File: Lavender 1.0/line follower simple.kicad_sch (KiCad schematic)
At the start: 51 parts, among them J1 XT60-M, J2 Conn_01x09_Pin, J3 Conn_01x02_Socket, J4 Conn_01x02_Socket, J5 Conn_01x09_Pin, J7 Conn_01x09_Socket, U10 QRE1113GR, U11 QRE1113GR, U12 STM32F411CEUx, U2 TCRT5000L, U3 QRE1113GR, U4 QRE1113GR, U5 QRE1113GR, U6 QRE1113GR, U7 QRE1113GR, U8 QRE1113GR, U9 QRE1113GR

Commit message: Added switches
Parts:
- removed BT1: ~, symbol customs:HC-05
- removed C10, C11, C18, C19, C20, C21, C22, C23, C9: 0.1u, symbol Device:C_Small
- removed J2: Conn_01x09_Pin, symbol Connector:Conn_01x09_Pin
- removed MP1: ~, symbol customs:MP1584
- removed R10, R12, R16, R18, R2, R4, R9: 220, symbol Device:R_Small
- removed R11, R13, R14, R15, R17, R3: 100, symbol Device:R_Small
- removed TB1: ~, symbol customs:tb6612_module
- removed U1: ~, symbol customs:Blackpill
- removed U12: STM32F411CEUx, Package_DFN_QFN:QFN-48-1EP_7x7mm_P0.5mm_EP5.6x5.6mm, symbol MCU_ST_STM32F4:STM32F411CEUx
- removed U3, U4, U5, U6, U7, U8, U9: QRE1113GR, QRE1113GR:SOIC180P460X187-4N, symbol customs:QRE1113GR
- added BT2: (no value), symbol customs:HC-05
- added JP1: SolderJumper_2_Open, symbol Jumper:SolderJumper_2_Open
- added MP2: (no value), symbol customs:MP1584
- added R24, R25, R27, R29, R32, R35, R38, R41, R44: 10k, symbol Device:R_Small
- added R26, R28, R31, R34, R37, R40, R43: 150, symbol Device:R_Small
- added R30, R33, R36, R39, R42, R45: 220, symbol Device:R_Small
- added SW1: SW_DPDT_x2, symbol Switch:SW_DPDT_x2
- added SW2: SW_Push, symbol Switch:SW_Push
- added TB2: (no value), symbol customs:tb6612_module
- added U1: YAAJ_BlackPill_Part_Like_SWD_Breakout, symbol customs:YAAJ_BlackPill_Part_Like_SWD_Breakout
- added U12, U13, U14, U15, U16, U17, U18: QRE1113GR, QRE1113GR:SOIC180P460X187-4N, symbol customs:QRE1113GR
- R21: value 100 -> 220
- R22, R23: value 100 -> 150
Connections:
- net +3.3V: now also BT2. (EN), MP2. (IN+), R24.2, R25.2, R26.2, R27.2, R28.2, R29.2, R31.2, R32.2, R34.2, R35.2, R37.2, R38.2, R40.2, R41.2, R43.2, R44.2, TB2. (M1Out+); no longer R21.2
- net BAT+: now also SW1.2 (B)
- net GND: now also BT2. (EN), MP2. (IN+), SW2.1, TB2. (M1Out+), U12.2, U12.4, U13.2, U13.4, U14.2, U14.4, U15.2, U15.4, U16.2, U16.4, U17.2, U17.4, U18.2, U18.4
- net Motor1+: now also TB2. (M1Out+)
- net Motor1-: now also TB2. (M1Out+)
- net Motor2+: now also TB2. (M1Out+)
- net Motor2-: now also TB2. (M1Out+)
- net PIN: now also BT2. (EN)
- net Q1: now also R19.1, JP1.1 (A); no longer J5.9 (Pin_9)
- net Q2: now also R20.1; no longer J5.8 (Pin_8)
- net Q3: now also R21.1; no longer J5.7 (Pin_7)
- net Q4: now also R30.1; no longer J5.6 (Pin_6)
- net Q5: now also R33.1; no longer J5.5 (Pin_5)
- net Q6: now also R36.1; no longer J5.4 (Pin_4)
- net Q7: now also R39.1; no longer J5.3 (Pin_3)
- net Q8: now also R42.1; no longer J5.2 (Pin_2), R19.1
- net Q9: now also R45.1; no longer J5.1 (Pin_1), R20.1
- net at R19.2, U10.3: now also R24.1
- net at R20.2, U11.3: now also R25.1
- net BAT_SNS renamed PB1
- net PB1: now also U1.32 (PB1)
- removed net Pin: J7.1 (Pin_1), J7.2 (Pin_2), J7.3 (Pin_3), J7.4 (Pin_4), J7.5 (Pin_5), J7.6 (Pin_6), J7.7 (Pin_7), J7.8 (Pin_8), J7.9 (Pin_9)
- new net: R32.1, R33.2, U14.3
- new net: R38.1, R39.2, U16.3
- new net: R40.1, U17.1
- new net: R29.1, R30.2, U13.3
- new net: R41.1, R42.2, U17.3
- new net: R26.1, U12.1
- new net: R43.1, U18.1
- new net: R44.1, R45.2, U18.3
- new net: R28.1, U13.1
- new net: R31.1, U14.1
- new net: R37.1, U16.1
- new net: J5.9 (Pin_9), JP1.2 (B)
- new net: R21.2, R27.1, U12.3
- new net: R34.1, U15.1
- new net: R35.1, R36.2, U15.3
- new net BAT+_Driver: SW1.4 (A), TB2. (M1Out+)
- new net BAT+_out: MP2. (IN+), SW1.1 (A), SW1.5 (B)
- new net PA0: J7.9 (Pin_9), U1.23 (PA0)
- new net PA1: J7.8 (Pin_8), U1.24 (PA1)
- new net PA10: BT2. (EN), U1.7 (PA10)
- new net PA11: TB2. (M1Out+), U1.8 (PA11)
- new net PA2: J7.7 (Pin_7), U1.25 (PA2)
- new net PA3: J7.6 (Pin_6), U1.26 (PA3)
- new net PA4: J7.5 (Pin_5), U1.27 (PA4)
- new net PA5: J7.4 (Pin_4), U1.28 (PA5)
- new net PA6: J7.3 (Pin_3), U1.29 (PA6)
- new net PA7: J7.2 (Pin_2), U1.30 (PA7)
- new net PA8: TB2. (M1Out+), U1.5 (PA8)
- new net PA9: BT2. (EN), U1.6 (PA9)
- new net PB0: J7.1 (Pin_1), U1.31 (PB0)
- new net PB12: TB2. (M1Out+), U1.1 (PB12)
- new net PB13: TB2. (M1Out+), U1.2 (PB13)
- new net PB14: TB2. (M1Out+), U1.3 (PB14)
- new net PB15: TB2. (M1Out+), U1.4 (PB15)
- new net PB4: SW2.2, U1.12 (PB4)
- no-connect marks 0 -> 6
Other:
- moved on the sheet: J5, J7, U2

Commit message: Completed schematic layout
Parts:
- removed J1: XT60-M, XT60-M:AMASS_XT60-M, symbol New_Library:XT60-M
- removed J5: Conn_01x09_Pin, symbol Connector:Conn_01x09_Pin
- removed J7: Conn_01x09_Socket, symbol Connector:Conn_01x09_Socket
- removed MP2: (no value), symbol customs:MP1584
- removed U1: YAAJ_BlackPill_Part_Like_SWD_Breakout, symbol customs:YAAJ_BlackPill_Part_Like_SWD_Breakout
- added BlackPill1: STM32F411_BP, ROBO:STM32F411-BP, symbol RM_Footprints:STM32F411-BlackPill
- added J1: XT30UPB-M, XT30UPB-M:AMASS_XT30UPB-M, symbol customs:XT30UPB-M
- added J6, J7: Conn_02x06_Counter_Clockwise, symbol Connector_Generic:Conn_02x06_Counter_Clockwise
- added JP10, JP11, JP12, JP13, JP14, JP15, JP16, JP17, JP18, JP19, JP2, JP20, JP3, JP4, JP5, JP6, JP7, JP8, JP9: SolderJumper_2_Open, symbol Jumper:SolderJumper_2_Open
- added MP1: (no value), symbol customs:MP1584
- added R49, R52, R55, R58, R61, R64, R67, R70, R73: 150, symbol Device:R_Small
- added R50, R53, R56, R59, R62, R65, R68, R71, R74: 4k7, symbol Device:R_Small
- added R51, R54, R57, R60, R63, R66, R69, R72, R75: 220, symbol Device:R_Small
- added U19, U20, U4, U5, U6, U7, U8, U9: TCRT5000L, TCRT5000L:XDCR_TCRT5000L, symbol customs:TCRT5000L
- added U3: 2472, 2472:MODULE_2472, symbol customs:2472
- R24, R25, R27, R29, R32, R35, R38, R41, R44: value 10k -> 4k7
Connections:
- net PA11 is gone; now on net PWMB: TB2. (M1Out+)
- net PA8 is gone; now on net PWMB: TB2. (M1Out+)
- net PA9 is gone; now on net TXD: BT2. (EN)
- net PB12 is gone; now on net PWMB: TB2. (M1Out+)
- net PB13 is gone; now on net PWMB: TB2. (M1Out+)
- net PB14 is gone; now on net PWMB: TB2. (M1Out+)
- net PB15 is gone; now on net PWMB: TB2. (M1Out+)
- net PIN is gone; now on net TXD: BT2. (EN)
- net +3.3V: now also BlackPill1.40 (3V3), J6.7 (Pin_7), J7.7 (Pin_7), JP19.2 (B), JP20.2 (B), MP1. (IN+), U3.1 (VIN); no longer R22.2, R23.2, R24.2, R25.2, R26.2, R27.2, R28.2, R29.2, R31.2, R32.2, R34.2, R35.2, R37.2, R38.2, R40.2, R41.2, R43.2, R44.2
- net BAT+: now also J1.P
- net BAT+_out: now also MP1. (IN+)
- net GND: now also U2.2, U2.3, BlackPill1.2 (GND), BlackPill1.39 (GND), J1.N, J6.6 (Pin_6), J7.6 (Pin_6), MP1. (IN+), U19.2, U19.3, U20.2, U20.3, U3.10 (PS0), U3.3 (GND), U3.7 (ADR), U3.9 (PS1), U4.2, U4.3, U5.2, U5.3, U6.2, U6.3, U7.2, U7.3, U8.2, U8.3, U9.2, U9.3
- net Q1: now also JP2.1 (A); no longer JP1.1 (A)
- net Q2: now also JP4.1 (A)
- net Q3: now also JP6.1 (A)
- net Q4: now also JP8.1 (A)
- net Q5: now also JP10.1 (A)
- net Q6: now also JP11.1 (A)
- net Q7: now also JP14.1 (A)
- net Q8: now also JP16.1 (A)
- net Q9: now also JP18.1 (A)
- net T1: now also JP1.1 (A), R51.2
- net T2: now also JP3.1 (A), R54.2
- net T3: now also JP5.1 (A), R57.2
- net T4: now also JP7.1 (A), R60.2
- net T5: now also JP9.1 (A), R63.2
- net T6: now also JP12.1 (A), R66.2
- net T7: now also JP13.1 (A), R69.2
- net T8: now also JP15.1 (A), R72.2
- net T9: now also JP17.1 (A), R75.2
- net at U2.1: now also R50.2, R51.1
- net at U2.4: now also R49.2
- net at JP1.2 (B): now also J6.1 (Pin_1), JP2.2 (B)
- net PWMB: now reaches TB2. (M1Out+)
- net PWMB: now also BlackPill1.28 (PA11)
- net PA10 renamed TXD
- net TXD: now also BlackPill1.27 (PA10)
- net PB1 renamed BAT_SNS
- net BAT_SNS: now also BlackPill1.6 (PB1)
- net PB4 renamed Button
- net Button: now also BlackPill1.32 (PB4)
- new net: J6.10 (Pin_10), JP15.2 (B), JP16.2 (B)
- new net: J6.11 (Pin_11), JP13.2 (B), JP14.2 (B)
- new net: R56.2, R57.1, U5.1
- new net: R55.2, U5.4
- new net: R68.2, R69.1, U9.1
- new net: J6.5 (Pin_5), JP10.2 (B), JP9.2 (B)
- new net: J6.3 (Pin_3), JP5.2 (B), JP6.2 (B)
- new net: R65.2, R66.1, U8.1
- new net: R64.2, U8.4
- new net: R67.2, U9.4
- new net: J6.12 (Pin_12), JP11.2 (B), JP12.2 (B)
- new net: R71.2, R72.1, U19.1
- new net: R70.2, U19.4
- new net: J6.2 (Pin_2), JP3.2 (B), JP4.2 (B)
- new net: J6.4 (Pin_4), JP7.2 (B), JP8.2 (B)
- new net: J6.9 (Pin_9), JP17.2 (B), JP18.2 (B)
- new net: R62.2, R63.1, U7.1
- new net: R61.2, U7.4
- new net: R74.2, R75.1, U20.1
- new net: R73.2, U20.4
- new net: R59.2, R60.1, U6.1
- new net: R58.2, U6.4
- new net: R53.2, R54.1, U4.1
- new net: R52.2, U4.4
- new net AIN1: BlackPill1.23 (PB14), TB2. (M1Out+)
- new net AIN2: BlackPill1.24 (PB15), TB2. (M1Out+)
- new net BIN1: BlackPill1.22 (PB13), TB2. (M1Out+)
- new net BIN2: BlackPill1.21 (PB12), TB2. (M1Out+)
- new net EN: BT2. (EN), BlackPill1.34 (PB6)
- new net IMU_RST: BlackPill1.4 (PB10), U3.6 (RST)
- new net IMU_SCL: BlackPill1.36 (PB8), U3.5 (SCL)
- new net IMU_SDA: BlackPill1.37 (PB9), U3.4 (SDA)
- new net PWMA: BlackPill1.25 (PA8), TB2. (M1Out+)
- new net Q_PWR: JP19.1 (A), R22.2, R23.2, R24.2, R25.2, R26.2, R27.2, R28.2, R29.2, R31.2, R32.2, R34.2, R35.2, R37.2, R38.2, R40.2, R41.2, R43.2, R44.2
- new net RXD: BT2. (EN), BlackPill1.26 (PA9)
- new net SNSR1: BlackPill1.15 (PA0), J7.1 (Pin_1)
- new net SNSR2: BlackPill1.14 (PA1), J7.2 (Pin_2)
- new net SNSR3: BlackPill1.13 (PA2), J7.3 (Pin_3)
- new net SNSR4: BlackPill1.12 (PA3), J7.4 (Pin_4)
- new net SNSR5: BlackPill1.11 (PA4), J7.5 (Pin_5)
- new net SNSR6: BlackPill1.10 (PA5), J7.12 (Pin_12)
- new net SNSR7: BlackPill1.9 (PA6), J7.11 (Pin_11)
- new net SNSR8: BlackPill1.8 (PA7), J7.10 (Pin_10)
- new net SNSR9: BlackPill1.7 (PB0), J7.9 (Pin_9)
- new net STATE: BT2. (EN), BlackPill1.33 (PB5)
- new net T_PWR: JP20.1 (A), R49.1, R50.1, R52.1, R53.1, R55.1, R56.1, R58.1, R59.1, R61.1, R62.1, R64.1, R65.1, R67.1, R68.1, R70.1, R71.1, R73.1, R74.1
- no-connect marks 6 -> 20
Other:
- note added: "BNO055 Module"
- note added: "Kill switches"
- note added: "MCU"
- note added: "Programming button"
- note added: "Sensor Power bus"
- note added: "TCRT5000L Sensors"
- moved on the sheet: BT2, C8, J3, J4, R19, R20, R21, R22, R23, R24, R25, R26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

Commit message: Fixed ERC error
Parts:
- removed C8: 22u, symbol Device:C_Small
- removed R19, R20, R21, R30, R33, R36, R39, R42, R45, R51, R54, R57, R60, R63, R66, R69, R72, R75: 220, symbol Device:R_Small
- removed R22, R23, R26, R28, R31, R34, R37, R40, R43, R49, R52, R55, R58, R61, R64, R67, R70, R73: 150, symbol Device:R_Small
- removed R24, R25, R27, R29, R32, R35, R38, R41, R44, R50, R53, R56, R59, R62, R65, R68, R71, R74: 4k7, symbol Device:R_Small
- removed TB2: (no value), symbol customs:tb6612_module
- removed U10, U11, U12, U13, U14, U15, U16, U17, U18: QRE1113GR, QRE1113GR:SOIC180P460X187-4N, symbol customs:QRE1113GR
- removed U19, U2, U20, U4, U5, U6, U7, U8, U9: TCRT5000L, TCRT5000L:XDCR_TCRT5000L, symbol customs:TCRT5000L
- removed U3: 2472, 2472:MODULE_2472, symbol customs:2472
- added C9: 22u, Capacitor_SMD:C_0603_1608Metric_Pad1.08x0.95mm_HandSolder, symbol Device:C_Small
- added D1, D2: LED, LED_THT:LED_D5.0mm, symbol Device:LED
- added R1, R2: 47, symbol Device:R
- added TB1: (no value), symbol customs:TB6612_module
- added U21: BNO055, ROBO:7_semi_BNO055, symbol RM_Footprints:BNO055_7Semi_Module
- BT2: footprint (none) -> Connector_PinSocket_2.54mm:PinSocket_1x06_P2.54mm_Vertical
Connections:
- net +3.3V: now also BT2.5 (VCC), MP1.7 (OUT+), MP1.8, C9.2, TB1.2 (VCC), U21.1 (Vin); no longer BT2. (EN), MP1. (IN+)
- net AIN1: now also TB1.8 (AIN1)
- net AIN2: now also TB1.9 (AIN2)
- net BAT+_Driver: now also TB1.1 (VM)
- net BAT+_out: now also MP1.3 (IN+), MP1.4; no longer MP1. (IN+)
- net BIN1: now also TB1.6 (BIN1)
- net BIN2: now also TB1.5 (BIN2)
- net EN: now also BT2.6 (EN); no longer BT2. (EN)
- net GND: now also BT2.4 (GND), MP1.1 (IN-), MP1.2, MP1.5 (OUT-), MP1.6, C9.1, D1.1 (K), D2.1 (K), TB1.13 (GND), TB1.14 (GND), TB1.3 (GND), U21.10 (ADD), U21.3 (GND), U21.7 (PS0), U21.8 (PS1); no longer BT2. (EN), MP1. (IN+)
- net IMU_RST: now also U21.6 (RST)
- net IMU_SCL: now also U21.5 (SCL)
- net IMU_SDA: now also U21.4 (SDA)
- net Motor1+: now also TB1.16 (M1Out+)
- net Motor1-: now also TB1.15 (M1Out-)
- net Motor2+: now also TB1.11 (M2Out+)
- net Motor2-: now also TB1.12 (M2Out-)
- net PWMA: now also TB1.10 (PWMA)
- net PWMB: now also TB1.4 (PWMB)
- net RXD: now also BT2.3 (RXD); no longer BT2. (EN)
- net STATE: now also BT2.1 (STATE); no longer BT2. (EN)
- net TXD: now also BT2.2 (TXD); no longer BT2. (EN)
- net LED: now reaches BlackPill1.30 (PA15)
- net LED: now also R1.2, R2.2
- new net: D2.2 (A), R2.1
- new net: D1.2 (A), R1.1
- no-connect marks 20 -> 19
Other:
- added sheet Sensors (untitled.kicad_sch)
- note added: "LEDs"
- note removed: "QRE1113 Sensors"
- note removed: "TCRT5000L Sensors"
- moved on the sheet: SW2

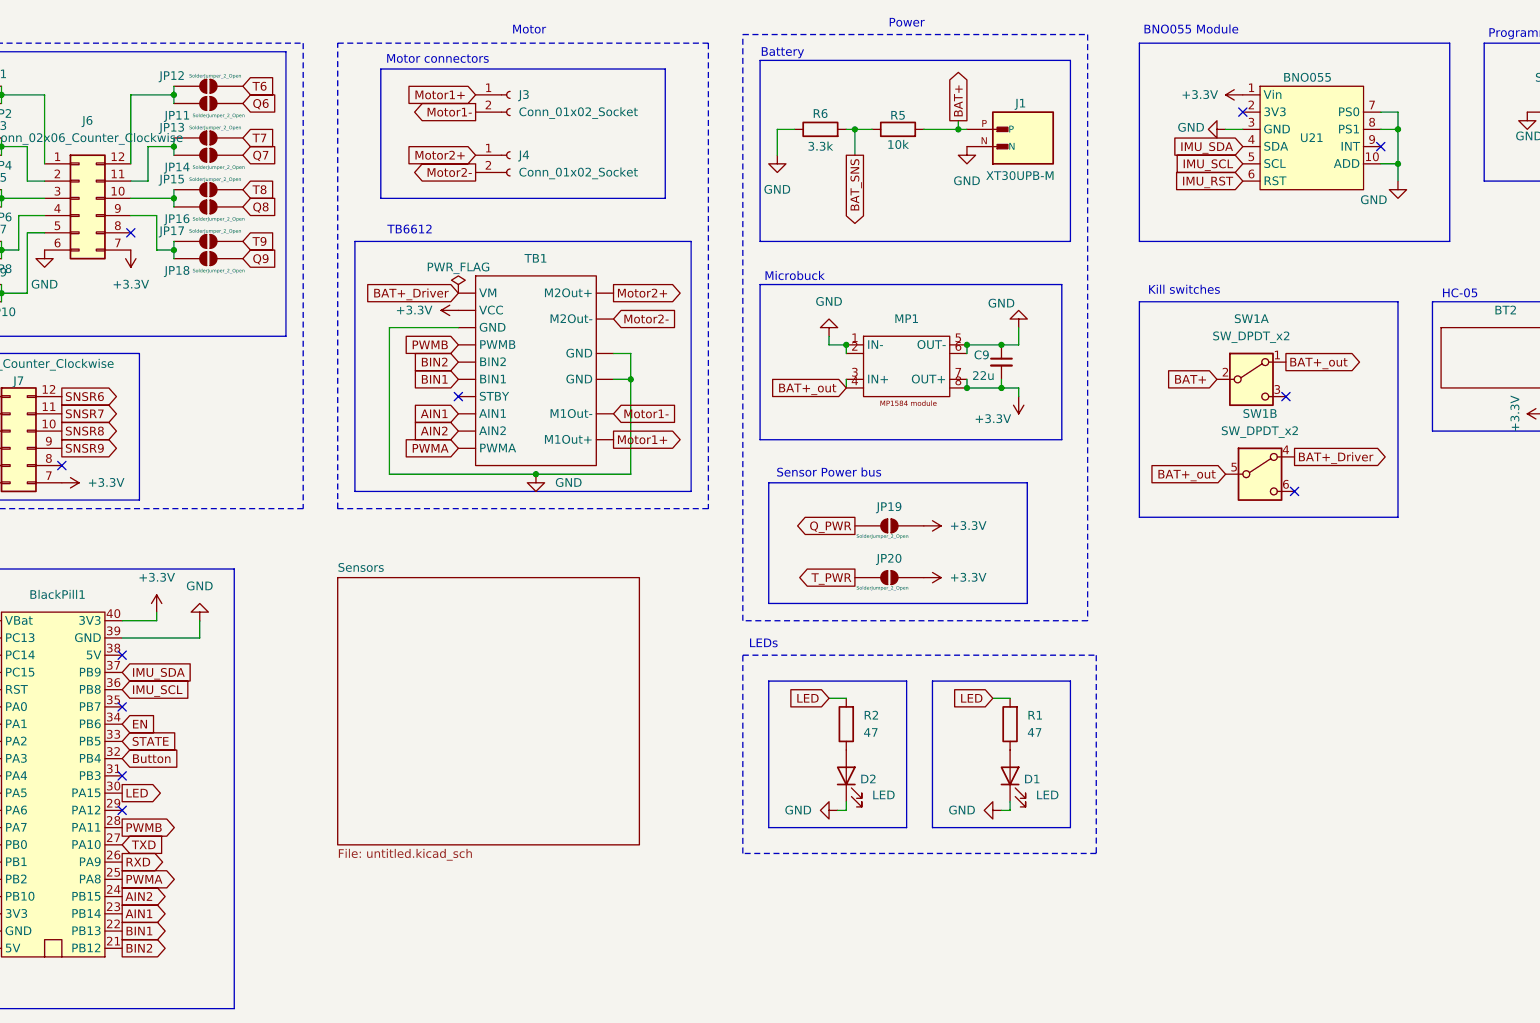
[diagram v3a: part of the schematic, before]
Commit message: arrange pcb components
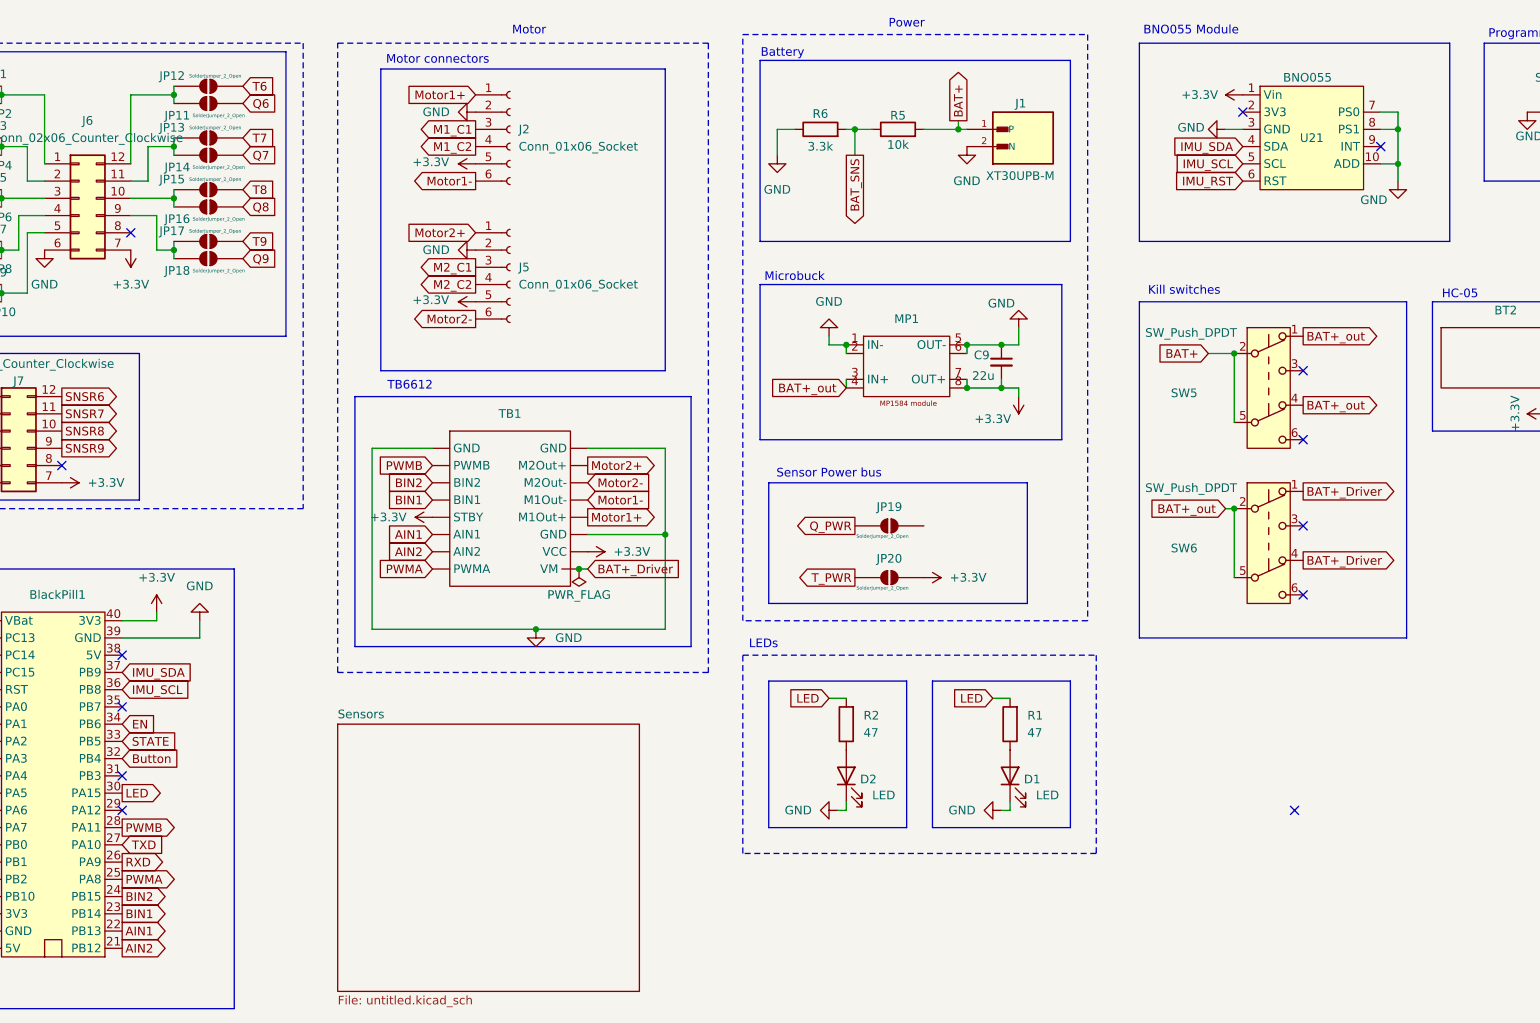
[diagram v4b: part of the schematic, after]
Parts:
- removed J3, J4: Conn_01x02_Socket, symbol Connector:Conn_01x02_Socket
- removed SW1: SW_DPDT_x2, symbol Switch:SW_DPDT_x2
- added J2, J5: Conn_01x06_Socket, Connector_JST:JST_SH_BM06B-SRSS-TB_1x06-1MP_P1.00mm_Vertical, symbol Connector:Conn_01x06_Socket
- added SW5, SW6: SW_Push_DPDT, Button_Switch_THT:SW_Push_2P2T_Toggle_CK_PVA2xxH3xxxxxxV2, symbol Switch:SW_Push_DPDT
- BlackPill1: footprint ROBO:STM32F411-BP -> customs:blackpill_fp
- J1: footprint XT30UPB-M:AMASS_XT30UPB-M -> Connector_AMASS:AMASS_XT30UPB-M_1x02_P5.0mm_Vertical
- J6, J7: footprint (none) -> Connector_IDC:IDC-Header_2x06_P2.54mm_Vertical_SMD
- JP1, JP10, JP11, JP12, JP13, JP14, JP15, JP16, JP17, JP18, JP19, JP2, JP20, JP3, JP4, JP5, JP6, JP7, JP8, JP9: footprint (none) -> Jumper:SolderJumper-2_P1.3mm_Open_RoundedPad1.0x1.5mm
- MP1: footprint (none) -> customs:MP1584_fp
- R1, R2, R5, R6: footprint (none) -> Resistor_SMD:R_0603_1608Metric_Pad0.98x0.95mm_HandSolder
- SW2: footprint (none) -> customs:Push button-fp
- TB1: footprint (none) -> customs:TB6612 module
- U21: footprint ROBO:7_semi_BNO055 -> customs:BNO055 module
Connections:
- net +3.3V: now also TB1.15 (VCC), TB1.5 (STBY), J2.5 (Pin_5), J5.5 (Pin_5); no longer JP19.2 (B), TB1.2 (VCC)
- net AIN1: now also BlackPill1.22 (PB13), TB1.6 (AIN1); no longer BlackPill1.23 (PB14), TB1.8 (AIN1)
- net AIN2: now also BlackPill1.21 (PB12), TB1.7 (AIN2); no longer BlackPill1.24 (PB15), TB1.9 (AIN2)
- net BAT+: now also J1.1 (P), SW5.2 (B), SW5.5 (B); no longer J1.P
- net BAT+_Driver: now also TB1.16 (VM), SW6.1 (A), SW6.4 (A); no longer TB1.1 (VM)
- net BAT+_out: now also SW5.1 (A), SW5.4 (A), SW6.2 (B), SW6.5 (B)
- net BIN1: now also BlackPill1.23 (PB14), TB1.4 (BIN1); no longer BlackPill1.22 (PB13), TB1.6 (BIN1)
- net BIN2: now also BlackPill1.24 (PB15), TB1.3 (BIN2); no longer BlackPill1.21 (PB12), TB1.5 (BIN2)
- net GND: now also J1.2 (N), TB1.1 (GND), TB1.9 (GND), J2.2 (Pin_2), J5.2 (Pin_2); no longer J1.N, TB1.13 (GND), TB1.3 (GND)
- net Motor1+: now also TB1.13 (M1Out+), J2.1 (Pin_1); no longer TB1.16 (M1Out+)
- net Motor1-: now also TB1.12 (M1Out-), J2.6 (Pin_6); no longer TB1.15 (M1Out-)
- net Motor2+: now also TB1.10 (M2Out+), J5.1 (Pin_1); no longer TB1.11 (M2Out+)
- net Motor2-: now also TB1.11 (M2Out-), J5.6 (Pin_6); no longer TB1.12 (M2Out-)
- net PWMA: now also TB1.8 (PWMA); no longer TB1.10 (PWMA)
- net PWMB: now also TB1.2 (PWMB); no longer TB1.4 (PWMB)
- new net M1_C1: J2.3 (Pin_3)
- new net M1_C2: J2.4 (Pin_4)
- new net M2_C1: J5.3 (Pin_3)
- new net M2_C2: J5.4 (Pin_4)
- no-connect marks 19 -> 21
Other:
- moved on the sheet: TB1
